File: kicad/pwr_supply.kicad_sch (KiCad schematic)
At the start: 20 parts

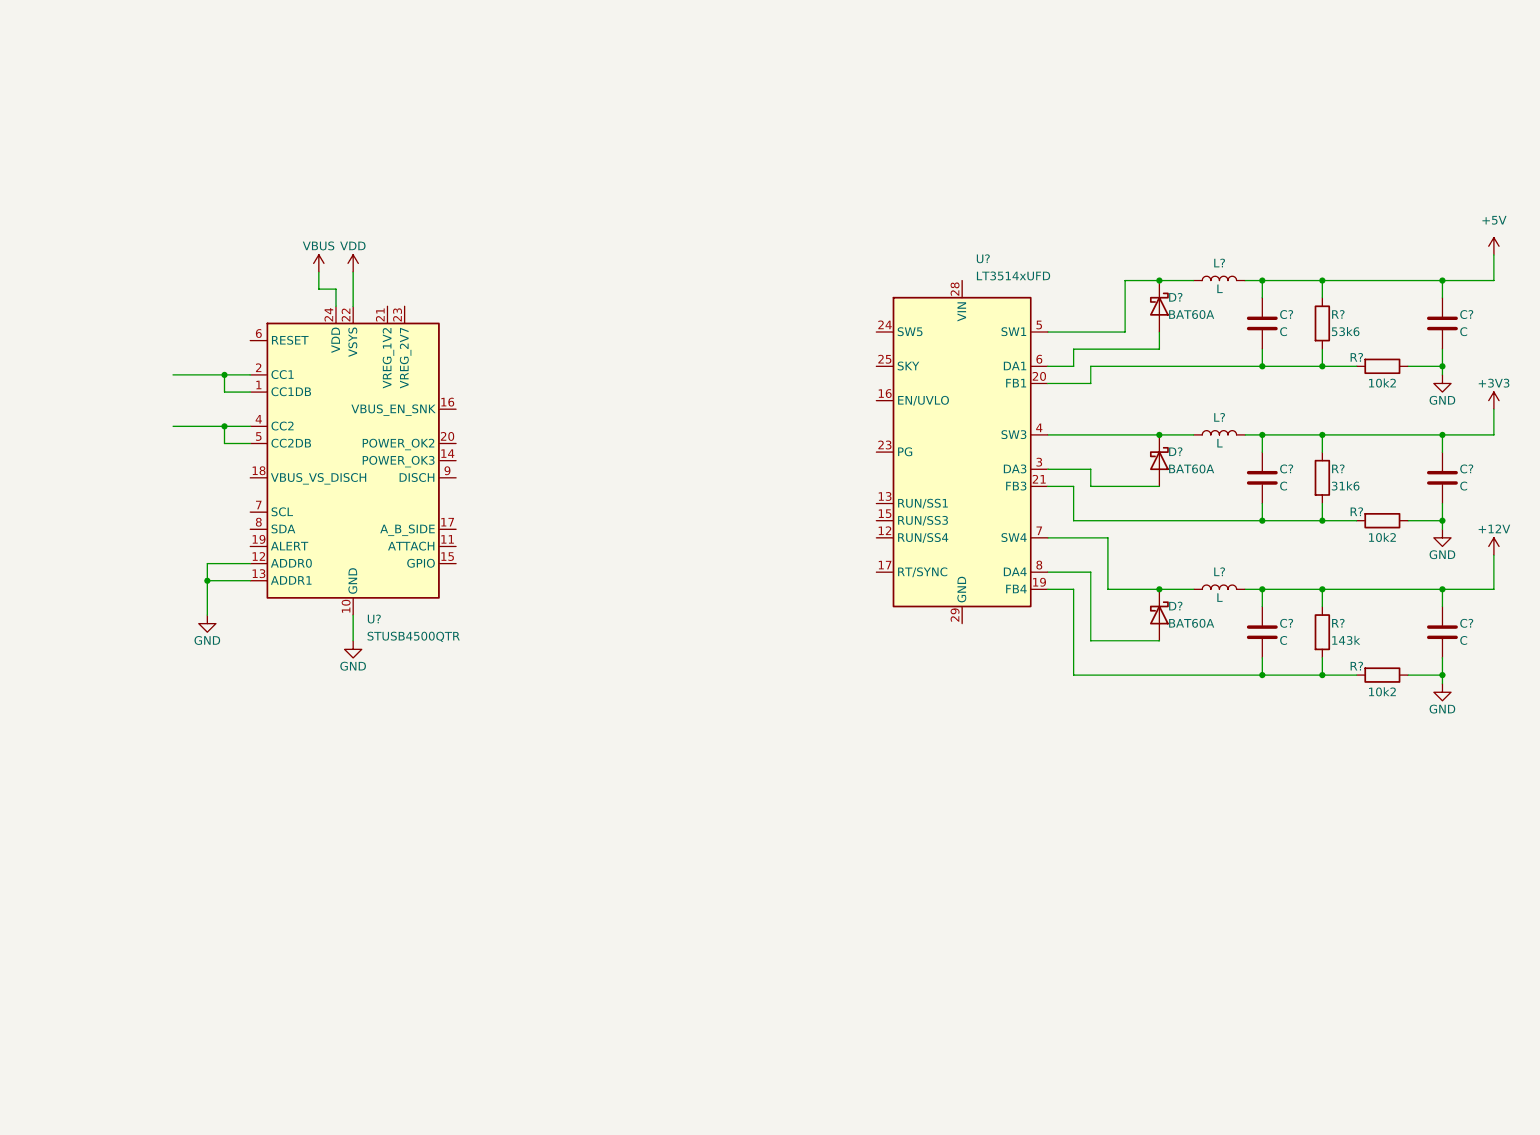
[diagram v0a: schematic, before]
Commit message: add all digikeys numbers to schematic
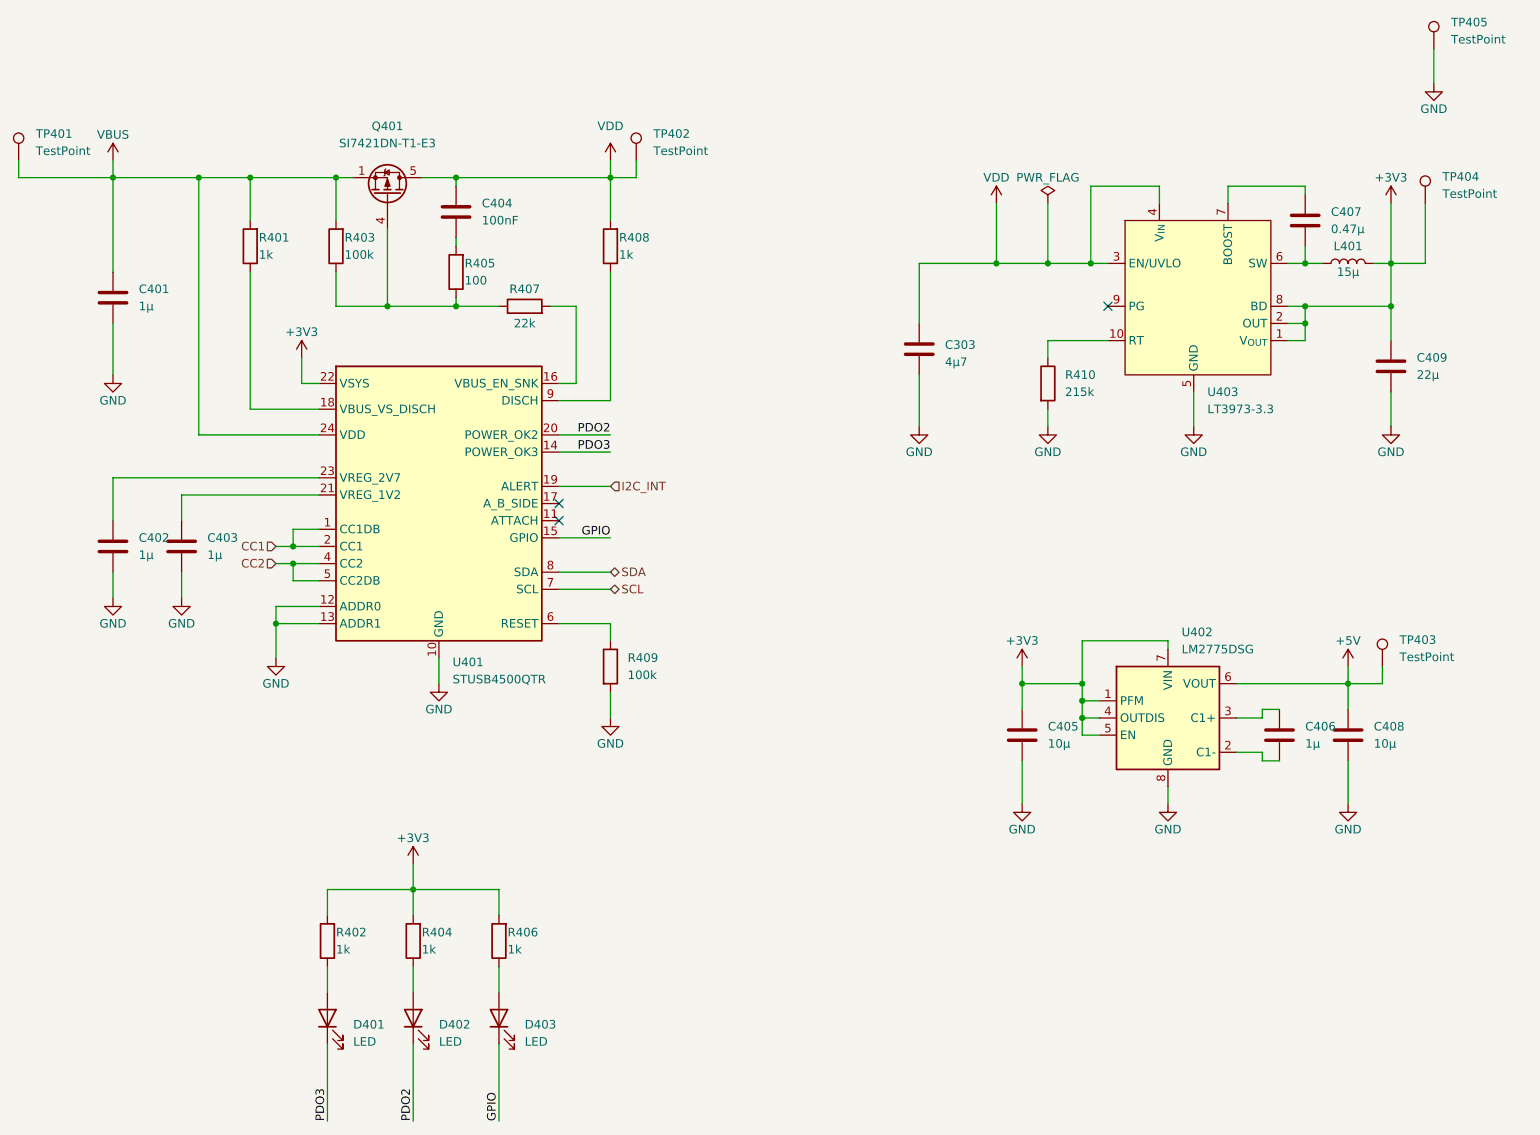
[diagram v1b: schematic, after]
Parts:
- removed C? (x6): C, symbol Device:C
- removed D? (x3): BAT60A, Diode_SMD:D_SOD-323, symbol Diode:BAT60A
- removed L? (x3): L, symbol Device:L
- removed R?: 53k6, Resistor_SMD:R_0805_2012Metric, symbol Device:R
- removed R? (x3): 10k2, Resistor_SMD:R_0805_2012Metric, symbol Device:R
- removed R?: 143k, Resistor_SMD:R_0805_2012Metric, symbol Device:R
- removed R?: 31k6, Resistor_SMD:R_0805_2012Metric, symbol Device:R
- removed U?: LT3514xUFD, Package_DFN_QFN:QFN-28-1EP_4x5mm_P0.5mm_EP2.65x3.65mm_ThermalVias, symbol Regulator_Switching:LT3514xUFD
- added C303: 4µ7, Capacitor_SMD:C_0603_1608Metric, symbol Device:C
- added C401, C402, C403, C406: 1µ, Capacitor_SMD:C_0603_1608Metric, symbol Device:C
- added C404: 100nF, Capacitor_SMD:C_0603_1608Metric, symbol Device:C
- added C405, C408: 10µ, Capacitor_SMD:C_0603_1608Metric, symbol Device:C
- added C407: 0.47µ, Capacitor_SMD:C_0603_1608Metric, symbol Device:C
- added C409: 22µ, Capacitor_SMD:C_0603_1608Metric, symbol Device:C
- added D401, D402, D403: LED, LED_SMD:LED_0603_1608Metric, symbol Device:LED
- added L401: 15µ, mylib_ic:L_TDK_VLS6045EX_VLS6045AF, symbol Device:L
- added Q401: SI7421DN-T1-E3, Package_SO:Vishay_PowerPAK_1212-8_Single, symbol mylib_ic:SI7421DN-T1-E3
- added R401, R402, R404, R406, R408: 1k, Resistor_SMD:R_0603_1608Metric, symbol Device:R
- added R403, R409: 100k, Resistor_SMD:R_0603_1608Metric, symbol Device:R
- added R405: 100, Resistor_SMD:R_0603_1608Metric, symbol Device:R
- added R407: 22k, Resistor_SMD:R_0603_1608Metric, symbol Device:R
- added R410: 215k, Resistor_SMD:R_0603_1608Metric, symbol Device:R
- added TP401, TP402, TP403, TP404, TP405: TestPoint, TestPoint:TestPoint_Keystone_5015_Micro-Minature, symbol Connector:TestPoint
- added U402: LM2775DSG, Package_SON:WSON-8-1EP_2x2mm_P0.5mm_EP0.9x1.6mm_ThermalVias, symbol Regulator_SwitchedCapacitor:LM2775DSG
- added U403: LT3973-3.3, Package_DFN_QFN:DFN-10-1EP_3x3mm_P0.5mm_EP1.65x2.38mm_ThermalVias, symbol mylib_ic:LT3973-3.3
- U401: renamed from U?; symbol Interface_USB:STUSB4500QTR -> mylib_ic:STUSB4500QTR; Digikey (none) -> 497-18060-1-ND
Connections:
- net +3V3: now also U401.22 (VSYS), C405.1, C409.1, L401.2, R402.2, R404.2, R406.2, TP404.1, U402.1 (PFM), U402.4 (OUTDIS), U402.5 (EN), U402.7 (VIN), U403.1 (V_{OUT}), U403.2 (OUT), U403.8 (BD)
- net +5V: now also C408.1, TP403.1, U402.6 (VOUT)
- net GND: now also C303.2, C401.2, C402.2, C403.2, C405.2, C408.2, C409.2, R409.2, R410.2, TP405.1, U402.8 (GND), U402.9 (GND), U403.11 (GND), U403.5 (GND)
- net VBUS: now also C401.1, Q401.1 (S), Q401.2 (S), Q401.3 (S), R401.2, R403.2, TP401.1
- net VDD: now also C303.1, C404.1, Q401.5 (D), R408.2, TP402.1, U403.3 (EN/UVLO), U403.4 (V_{IN}); no longer U401.22 (VSYS)
- net CC1: now reaches U401.1 (CC1DB), U401.2 (CC1)
- net PDO3: now reaches U401.14 (POWER_OK3)
- net PDO3: now also D401.1 (K)
- net GPIO: now reaches U401.15 (GPIO)
- net GPIO: now also D403.1 (K)
- net at U401.16 (VBUS_EN_SNK): now also R407.2
- net at U401.18 (VBUS_VS_DISCH): now also R401.1
- net I2C_INT: now reaches U401.19 (ALERT)
- net PDO2: now reaches U401.20 (POWER_OK2)
- net PDO2: now also D402.1 (K)
- net at U401.21 (VREG_1V2): now also C403.1
- net at U401.23 (VREG_2V7): now also C402.1
- net CC2: now reaches U401.4 (CC2), U401.5 (CC2DB)
- net at U401.6 (RESET): now also R409.1
- net SCL: now reaches U401.7 (SCL)
- net SDA: now reaches U401.8 (SDA)
- net at U401.9 (DISCH): now also R408.1
- new net: D401.2 (A), R402.1
- new net: R410.1, U403.10 (RT)
- new net: C407.2, L401.1, U403.6 (SW)
- new net: C407.1, U403.7 (BOOST)
- new net: D403.2 (A), R406.1
- new net: D402.2 (A), R404.1
- new net: C406.1, U402.2 (C1-)
- new net: C406.2, U402.3 (C1+)
- new net: Q401.4 (G), R403.1, R405.1, R407.1
- new net: C404.2, R405.2
- no-connect marks 0 -> 3
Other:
- moved on the sheet: U401

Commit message: wip
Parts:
- U402: renamed from U401; footprint Package_DFN_QFN:QFN-24-1EP_4x4mm_P0.5mm_EP2.7x2.7mm -> Package_DFN_QFN:QFN-24-1EP_4x4mm_P0.5mm_EP2.7x2.7mm_ThermalVias
- renumbered C404 to C401, C407 to C402, C401 to C403, C409 to C405, C402 to C406, C403 to C407, C405 to C408, C406 to C409, C408 to C410, R403 to R402, R408 to R403, R405 to R404, R407 to R405, R410 to R406, R409 to R407, R402 to R408, R404 to R409, R406 to R410, TP405 to TP401, TP401 to TP402, TP402 to TP403, TP403 to TP405, U403 to U401, U402 to U403

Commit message: add nrf52840 board
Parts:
- C303: Digikey (none) -> 478-06033D475KAT2ACT-ND
- U401: Digikey LT3973IDD-5#PBF-ND -> LT3973IDD-3.3#PBF-ND
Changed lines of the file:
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@@
       (effects (font (size 1.27 1.27)) hide)
     )
-    (property "Digikey" "LT3973IDD-5#PBF-ND" (at 205.74 60.96 0)
+    (property "Digikey" "LT3973IDD-3.3#PBF-ND" (at 205.74 60.96 0)
       (effects (font (size 1.27 1.27)) hide)
     )
@@
       (effects (font (size 1.27 1.27)) hide)
     )
-    (property "Digikey" "" (at 165.1 68.58 0)
+    (property "Digikey" "478-06033D475KAT2ACT-ND" (at 165.1 68.58 0)
       (effects (font (size 1.27 1.27)) hide)
     )
@@
   (symbol (lib_id "mylib_ic:STUSB4500QTR") (at 93.98 91.44 0) (unit 1)
     (in_bom yes) (on_board yes) (dnp no) (fields_autoplaced)
-    (property "Reference" "U402" (at 95.9994 114.935 0)
-      (effects (font (size 1.27 1.27)) (justify left))
-    )
-    (property "Value" "STUSB4500QTR" (at 95.9994 117.475 0)
-      (effects (font (size 1.27 1.27)) (justify left))
+    (property "Reference" "U402" (at 93.98 67.31 0)
+      (effects (font (size 1.27 1.27)))
+    )
+    (property "Value" "STUSB4500QTR" (at 93.98 69.85 0)
+      (effects (font (size 1.27 1.27)))
     )
     (property "Footprint" "Package_DFN_QFN:QFN-24-1EP_4x4mm_P0.5mm_EP2.7x2.7mm_ThermalVias" (at 93.98 91.44 0)

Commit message: rework board
add nrf 7002
add oled display
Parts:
- removed D403: LED, LED_SMD:LED_0603_1608Metric, symbol Device:LED
- removed R410: 1k, Resistor_SMD:R_0603_1608Metric, symbol Device:R
- C406, C407: footprint Capacitor_SMD:C_0603_1608Metric -> Capacitor_SMD:C_0402_1005Metric; Digikey CL10A105KA8NNNC -> 1276-1067-2-ND
- Q401: footprint Package_SO:Vishay_PowerPAK_1212-8_Single -> mylib_ic:Vishay_PowerPAK_1212-8_Single
- R407: footprint Resistor_SMD:R_0603_1608Metric -> Resistor_SMD:R_0402_1005Metric; Digikey 311-100KHRCT-ND -> 1292-WR04X1003FTLTR-ND
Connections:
- net GPIO: no longer names the net of U402.15 (GPIO)
- no-connect marks 3 -> 4
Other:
- title: (none) -> Firewaterburn
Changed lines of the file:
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@@
 (kicad_sch (version 20230121) (generator eeschema)
   (paper "A4")
+  (title_block
+    (title "Firewaterburn")
+    (rev "0.2")
+  )
   (junction (at 222.25 62.23) (diameter 0) (color 0 0 0 0)
   )
-  (junction (at 90.17 148.59) (diameter 0) (color 0 0 0 0)
-  )
   (junction (at 222.25 64.77) (diameter 0) (color 0 0 0 0)
   )
@@
   )
   (junction (at 222.25 55.88) (diameter 0) (color 0 0 0 0)
+  )
+  (junction (at 83.82 148.59) (diameter 0) (color 0 0 0 0)
   )
   (junction (at 72.39 97.79) (diameter 0) (color 0 0 0 0)
@@
   (no_connect (at 111.76 93.98))
   (no_connect (at 111.76 91.44))
+  (no_connect (at 111.76 96.52))
   (no_connect (at 193.04 62.23))
   (wire (pts (xy 76.2 77.47) (xy 66.04 77.47))
@@
     (stroke (width 0) (type default))
   )
+  (wire (pts (xy 83.82 148.59) (xy 90.17 148.59))
+    (stroke (width 0) (type default))
+  )
   (wire (pts (xy 212.09 118.11) (xy 228.6 118.11))
     (stroke (width 0) (type default))
@@
     (stroke (width 0) (type default))
   )
-  (wire (pts (xy 111.76 96.52) (xy 119.38 96.52))
-    (stroke (width 0) (type default))
-  )
   (wire (pts (xy 180.34 118.11) (xy 180.34 121.92))
     (stroke (width 0) (type default))
@@
     (stroke (width 0) (type default))
   )
-  (wire (pts (xy 77.47 148.59) (xy 90.17 148.59))
+  (wire (pts (xy 77.47 148.59) (xy 83.82 148.59))
     (stroke (width 0) (type default))
   )
@@
     (stroke (width 0) (type default))
   )
-  (wire (pts (xy 102.87 160.02) (xy 102.87 163.83))
-    (stroke (width 0) (type default))
-  )
   (wire (pts (xy 45.72 87.63) (xy 45.72 93.98))
     (stroke (width 0) (type default))
@@
     (stroke (width 0) (type default))
   )
-  (wire (pts (xy 102.87 171.45) (xy 102.87 182.88))
-    (stroke (width 0) (type default))
-  )
   (wire (pts (xy 241.3 24.13) (xy 241.3 29.21))
     (stroke (width 0) (type default))
@@
     (stroke (width 0) (type default))
   )
-  (wire (pts (xy 102.87 148.59) (xy 102.87 152.4))
-    (stroke (width 0) (type default))
-  )
   (wire (pts (xy 76.2 109.22) (xy 69.85 109.22))
     (stroke (width 0) (type default))
@@
     (stroke (width 0) (type default))
   )
-  (wire (pts (xy 90.17 148.59) (xy 102.87 148.59))
-    (stroke (width 0) (type default))
-  )
   (wire (pts (xy 90.17 152.4) (xy 90.17 148.59))
     (stroke (width 0) (type default))
@@
     (stroke (width 0) (type default))
   )
-  (wire (pts (xy 90.17 144.78) (xy 90.17 148.59))
+  (wire (pts (xy 83.82 144.78) (xy 83.82 148.59))
     (stroke (width 0) (type default))
   )
@@
   (wire (pts (xy 111.76 76.2) (xy 119.38 76.2))
     (stroke (width 0) (type default))
-  )
-  (label "GPIO" (at 119.38 96.52 180) (fields_autoplaced)
-    (effects (font (size 1.27 1.27)) (justify right bottom))
   )
   (label "PDO3" (at 119.38 83.82 180) (fields_autoplaced)
@@
   )
   (label "PDO2" (at 90.17 182.88 90) (fields_autoplaced)
-    (effects (font (size 1.27 1.27)) (justify left bottom))
-  )
-  (label "GPIO" (at 102.87 182.88 90) (fields_autoplaced)
     (effects (font (size 1.27 1.27)) (justify left bottom))
   )
@@
   )
   (symbol (lib_id "Device:C") (at 55.88 97.79 0) (unit 1)
-    (in_bom yes) (on_board yes) (dnp no) (fields_autoplaced)
-    (property "Reference" "C407" (at 59.69 96.5199 0)
-      (effects (font (size 1.27 1.27)) (justify left))
-    )
-    (property "Value" "1µ" (at 59.69 99.0599 0)
-      (effects (font (size 1.27 1.27)) (justify left))
-    )
-    (property "Footprint" "Capacitor_SMD:C_0603_1608Metric" (at 56.8452 101.6 0)
+    (in_bom yes) (on_board yes) (dnp no)
+    (property "Reference" "C407" (at 58.42 96.52 0)
+      (effects (font (size 1.27 1.27)) (justify left))
+    )
+    (property "Value" "1µ" (at 58.42 99.06 0)
+      (effects (font (size 1.27 1.27)) (justify left))
+    )
+    (property "Footprint" "Capacitor_SMD:C_0402_1005Metric" (at 56.8452 101.6 0)
       (effects (font (size 1.27 1.27)) hide)
     )
@@
       (effects (font (size 1.27 1.27)) hide)
     )
-    (property "Digikey" "CL10A105KA8NNNC" (at 55.88 97.79 0)
+    (property "Digikey" "1276-1067-2-ND" (at 55.88 97.79 0)
       (effects (font (size 1.27 1.27)) hide)
     )
@@
     )
   )
-  (symbol (lib_id "Device:R") (at 102.87 156.21 180) (unit 1)
-    (in_bom yes) (on_board yes) (dnp no)
-    (property "Reference" "R410" (at 104.14 154.94 0)
-      (effects (font (size 1.27 1.27)) (justify right))
-    )
-    (property "Value" "1k" (at 104.14 157.48 0)
-      (effects (font (size 1.27 1.27)) (justify right))
-    )
-    (property "Footprint" "Resistor_SMD:R_0603_1608Metric" (at 104.648 156.21 90)
-      (effects (font (size 1.27 1.27)) hide)
-    )
-    (property "Datasheet" "~" (at 102.87 156.21 0)
-      (effects (font (size 1.27 1.27)) hide)
-    )
-    (property "Digikey" "RNCP0603FTD1K00" (at 102.87 156.21 0)
-      (effects (font (size 1.27 1.27)) hide)
-    )
-    (pin "1")
-    (pin "2")
-    (instances
-      (project "firewaterburn"
-        (path "/e63e39d7-6ac0-4ffd-8aa3-1841a4541b55/da8e08cc-b8fa-44d2-9f6f-15fecbf9ecc5"
-          (reference "R410") (unit 1)
-        )
-      )
-    )
-  )
   (symbol (lib_id "Device:C") (at 222.25 49.53 0) (unit 1)
     (in_bom yes) (on_board yes) (dnp no)
@@
     )
   )
-  (symbol (lib_id "power:+3V3") (at 90.17 144.78 0) (unit 1)
-    (in_bom yes) (on_board yes) (dnp no)
-    (property "Reference" "#PWR0422" (at 90.17 148.59 0)
-      (effects (font (size 1.27 1.27)) hide)
-    )
-    (property "Value" "+3V3" (at 90.17 140.97 0)
-      (effects (font (size 1.27 1.27)))
-    )
-    (property "Footprint" "" (at 90.17 144.78 0)
-      (effects (font (size 1.27 1.27)) hide)
-    )
-    (property "Datasheet" "" (at 90.17 144.78 0)
+  (symbol (lib_id "power:+3V3") (at 83.82 144.78 0) (unit 1)
+    (in_bom yes) (on_board yes) (dnp no)
+    (property "Reference" "#PWR0422" (at 83.82 148.59 0)
+      (effects (font (size 1.27 1.27)) hide)
+    )
+    (property "Value" "+3V3" (at 83.82 140.97 0)
+      (effects (font (size 1.27 1.27)))
+    )
+    (property "Footprint" "" (at 83.82 144.78 0)
+      (effects (font (size 1.27 1.27)) hide)
+    )
+    (property "Datasheet" "" (at 83.82 144.78 0)
       (effects (font (size 1.27 1.27)) hide)
     )
@@
       (effects (font (size 1.27 1.27)) (justify left))
     )
-    (property "Footprint" "Resistor_SMD:R_0603_1608Metric" (at 117.602 115.57 90)
+    (property "Footprint" "Resistor_SMD:R_0402_1005Metric" (at 117.602 115.57 90)
       (effects (font (size 1.27 1.27)) hide)
     )
@@
       (effects (font (size 1.27 1.27)) hide)
     )
-    (property "Digikey" "311-100KHRCT-ND" (at 119.38 115.57 0)
+    (property "Digikey" "1292-WR04X1003FTLTR-ND" (at 119.38 115.57 0)
       (effects (font (size 1.27 1.27)) hide)
     )
@@
   )
   (symbol (lib_id "Device:C") (at 45.72 60.96 0) (unit 1)
-    (in_bom yes) (on_board yes) (dnp no) (fields_autoplaced)
+    (in_bom yes) (on_board yes) (dnp no)
     (property "Reference" "C403" (at 49.53 59.6899 0)
-      (effects (font (size 1.27 1.27)) (justify left))
+      (effects (font (size 1.27 1.27)) (justify right))
     )
     (property "Value" "1µ" (at 49.53 62.2299 0)
@@
       (effects (font (size 1.27 1.27)))
     )
-    (property "Footprint" "Package_SO:Vishay_PowerPAK_1212-8_Single" (at 88.9 40.64 0)
+    (property "Footprint" "mylib_ic:Vishay_PowerPAK_1212-8_Single" (at 88.9 40.64 0)
       (effects (font (size 1.27 1.27)) hide)
     )
@@
     )
   )
-  (symbol (lib_id "Device:LED") (at 102.87 167.64 90) (unit 1)
-    (in_bom yes) (on_board yes) (dnp no) (fields_autoplaced)
-    (property "Reference" "D403" (at 106.68 168.5925 90)
-      (effects (font (size 1.27 1.27)) (justify right))
-    )
-    (property "Value" "LED" (at 106.68 171.1325 90)
-      (effects (font (size 1.27 1.27)) (justify right))
-    )
-    (property "Footprint" "LED_SMD:LED_0603_1608Metric" (at 102.87 167.64 0)
-      (effects (font (size 1.27 1.27)) hide)
-    )
-    (property "Datasheet" "~" (at 102.87 167.64 0)
-      (effects (font (size 1.27 1.27)) hide)
-    )
-    (property "Digikey" "516-HSMS-C197CT-ND" (at 102.87 167.64 90)
-      (effects (font (size 1.27 1.27)) hide)
-    )
-    (pin "1")
-    (pin "2")
-    (instances
-      (project "firewaterburn"
-        (path "/e63e39d7-6ac0-4ffd-8aa3-1841a4541b55/da8e08cc-b8fa-44d2-9f6f-15fecbf9ecc5"
-          (reference "D403") (unit 1)
-        )
-      )
-    )
-  )
   (symbol (lib_id "power:+5V") (at 228.6 115.57 0) (unit 1)
     (in_bom yes) (on_board yes) (dnp no)
@@
   )
   (symbol (lib_id "Device:C") (at 45.72 97.79 0) (unit 1)
-    (in_bom yes) (on_board yes) (dnp no) (fields_autoplaced)
-    (property "Reference" "C406" (at 49.53 96.5199 0)
-      (effects (font (size 1.27 1.27)) (justify left))
-    )
-    (property "Value" "1µ" (at 49.53 99.0599 0)
-      (effects (font (size 1.27 1.27)) (justify left))
-    )
-    (property "Footprint" "Capacitor_SMD:C_0603_1608Metric" (at 46.6852 101.6 0)
+    (in_bom yes) (on_board yes) (dnp no)
+    (property "Reference" "C406" (at 48.26 96.52 0)
+      (effects (font (size 1.27 1.27)) (justify left))
+    )
+    (property "Value" "1µ" (at 48.26 99.06 0)
+      (effects (font (size 1.27 1.27)) (justify left))
+    )
+    (property "Footprint" "Capacitor_SMD:C_0402_1005Metric" (at 46.6852 101.6 0)
       (effects (font (size 1.27 1.27)) hide)
     )
@@
       (effects (font (size 1.27 1.27)) hide)
     )
-    (property "Digikey" "CL10A105KA8NNNC" (at 45.72 97.79 0)
-      (effects (font (size 1.27 1.27)) hide)
-    )
+    (property "Digikey" "1276-1067-2-ND" (at 45.72 97.79 0)
+      (effects (font (size 1.27 1.27)) hide)
+    )
